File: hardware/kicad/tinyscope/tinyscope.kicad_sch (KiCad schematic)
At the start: 4 parts, among them J1 USB_C_Receptacle_USB2.0, U1 USBLC6-2SC6_MOD

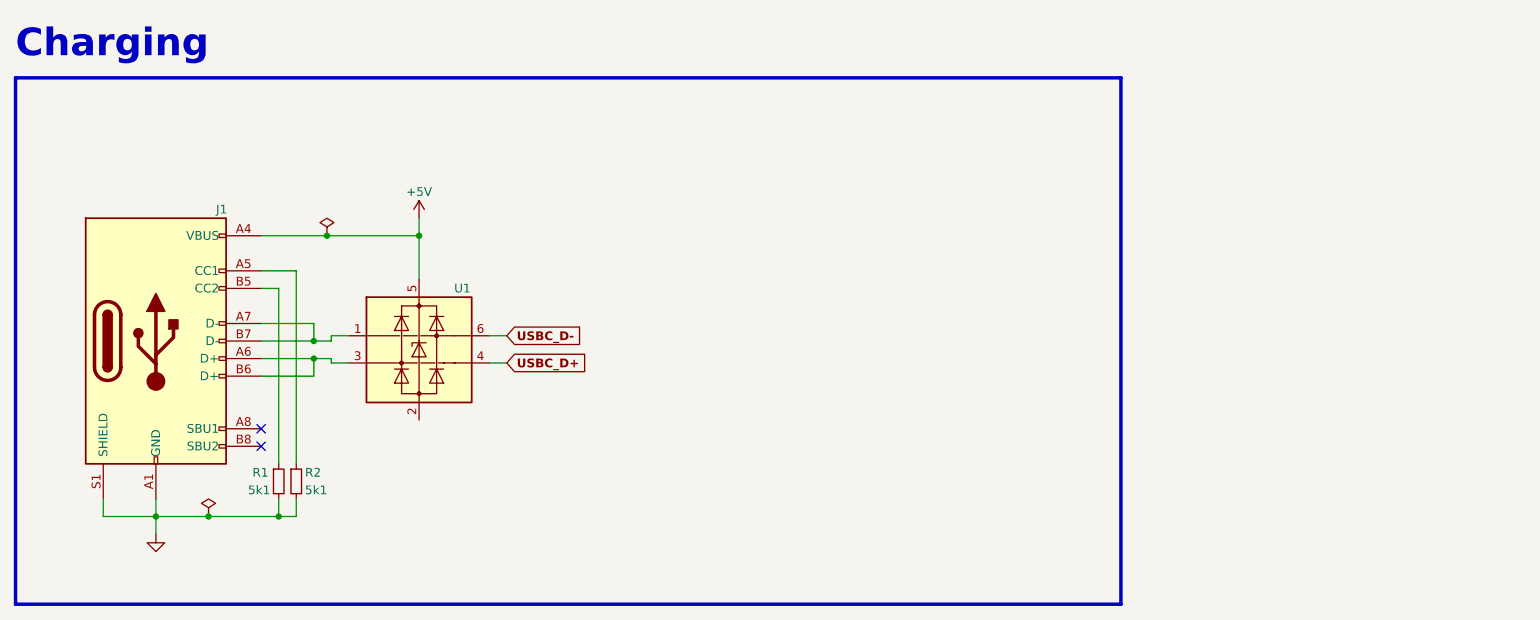
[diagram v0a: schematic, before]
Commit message: feat: hardware: Add tinyscope kicad project. Add USBC friendly battery charger part
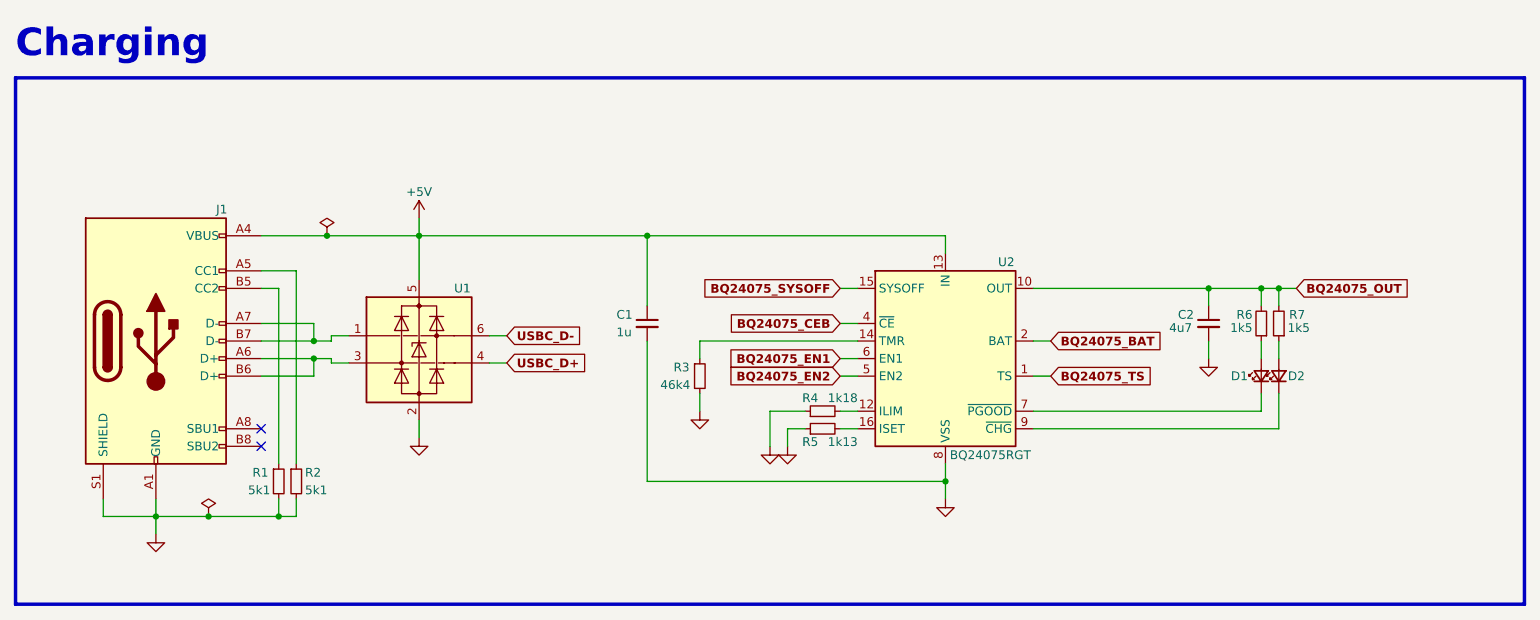
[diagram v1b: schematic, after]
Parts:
- added C1: 1u, symbol Device:C_Small
- added C2: 4u7, symbol Device:C_Small
- added D1, D2: LED_Small, symbol Device:LED_Small
- added R3: 46k4, symbol Device:R_Small
- added R4: 1k18, symbol Device:R_Small
- added R5: 1k13, symbol Device:R_Small
- added R6, R7: 1k5, symbol Device:R_Small
- added U2: BQ24075RGT, Package_DFN_QFN:VQFN-16-1EP_3x3mm_P0.5mm_EP1.6x1.6mm, symbol Battery_Management:BQ24075RGT
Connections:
- net +5V: now also C1.1, U2.13 (IN)
- net GND: now also U1.2 (GND), C1.2, C2.2, R3.2, R4.1, R5.1, U2.17 (VSS), U2.8 (VSS)
- new net: R5.2, U2.16 (ISET)
- new net: R4.2, U2.12 (ILIM)
- new net: R3.1, U2.14 (TMR)
- new net: D1.1 (K), U2.7 (~{PGOOD})
- new net: D2.1 (K), U2.9 (~{CHG})
- new net: D1.2 (A), R6.1
- new net: D2.2 (A), R7.1
- new net BQ24075_BAT: U2.2 (BAT), U2.3 (BAT)
- new net BQ24075_CEB: U2.4 (~{CE})
- new net BQ24075_EN1: U2.6 (EN1)
- new net BQ24075_EN2: U2.5 (EN2)
- new net BQ24075_OUT: C2.1, R6.2, R7.2, U2.10 (OUT), U2.11 (OUT)
- new net BQ24075_SYSOFF: U2.15 (SYSOFF)
- new net BQ24075_TS: U2.1 (TS)

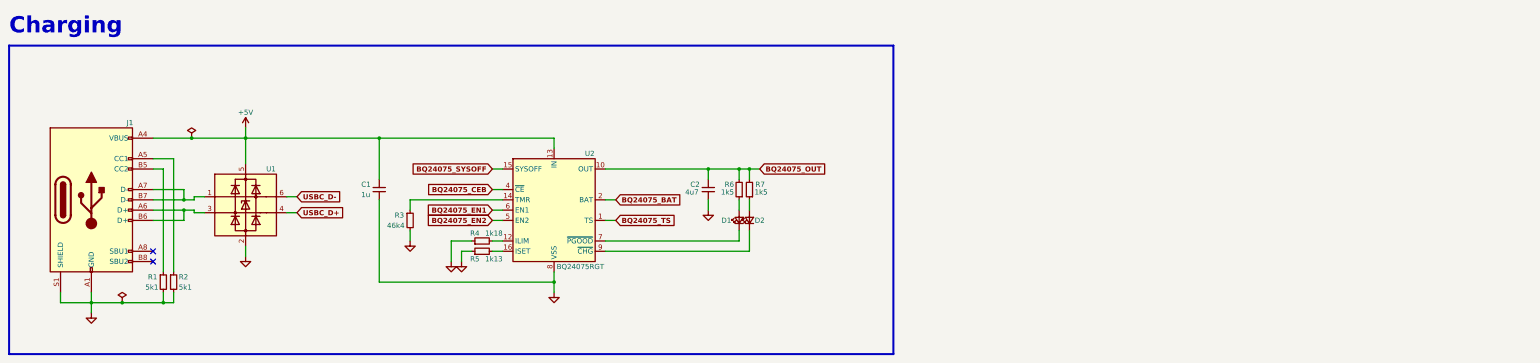
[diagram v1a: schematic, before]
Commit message: feat: hardware: Add tinyscope kicad project. Add fuel gauge part
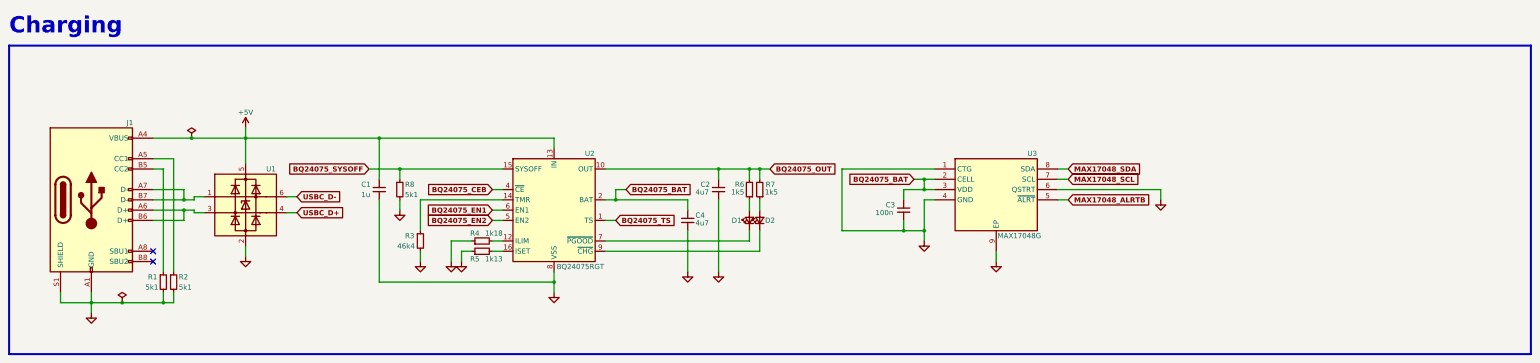
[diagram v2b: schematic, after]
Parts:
- added C3: 100n, symbol Device:C_Small
- added C4: 4u7, symbol Device:C_Small
- added R8: 5k1, symbol Device:R_Small
- added U3: MAX17048G, SON50P200X200X80-9N-D, symbol MAX17048G+T10:MAX17048G+T10
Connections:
- net BQ24075_BAT: now also C3.1, C4.1, U3.2 (CELL), U3.3 (VDD)
- net BQ24075_SYSOFF: now also R8.1
- net GND: now also C3.2, C4.2, R8.2, U3.1 (CTG), U3.4 (GND), U3.6 (QSTRT), U3.9 (EP)
- new net MAX17048_ALRTB: U3.5 (~{ALRT})
- new net MAX17048_SCL: U3.7 (SCL)
- new net MAX17048_SDA: U3.8 (SDA)
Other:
- moved on the sheet: C2, D1, D2, R3, R6, R7

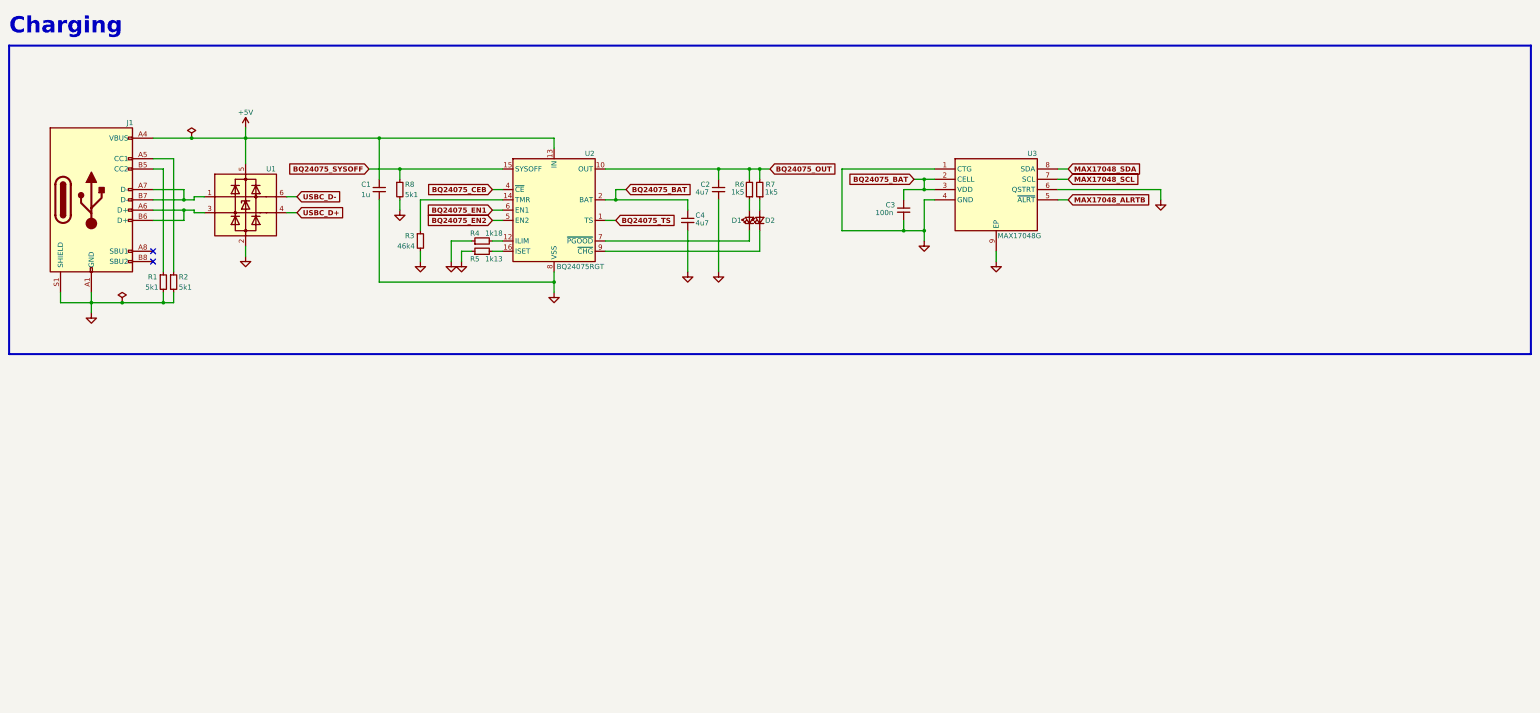
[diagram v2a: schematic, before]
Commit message: feat: hardware: Add tinyscope kicad project. Replace global labels with net labels
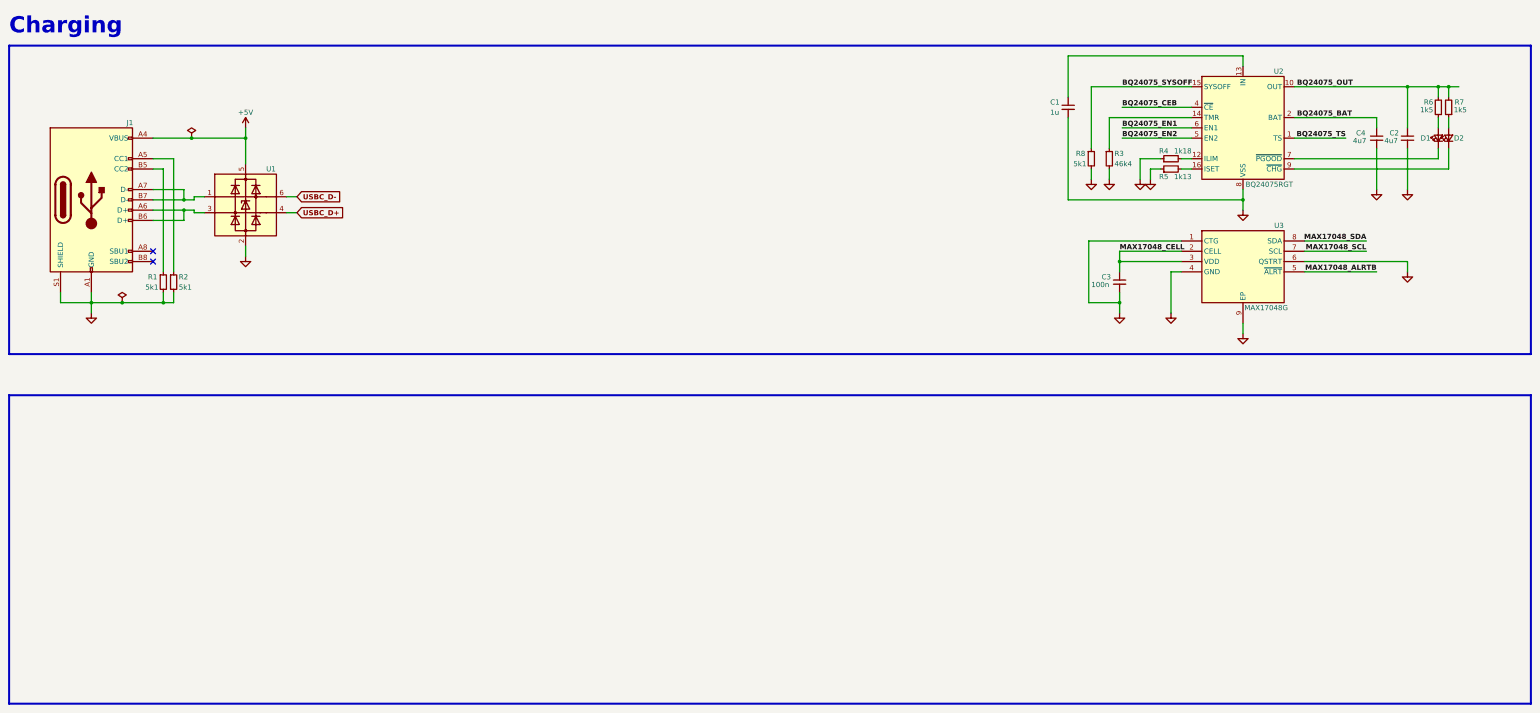
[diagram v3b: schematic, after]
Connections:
- net +5V: no longer C1.1, U2.13 (IN)
- net BQ24075_BAT: no longer C3.1, U3.2 (CELL), U3.3 (VDD)
- new net: C1.1, U2.13 (IN)
- new net MAX17048_CELL: C3.1, U3.2 (CELL), U3.3 (VDD)
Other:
- moved on the sheet: C1, C2, C3, C4, D1, D2, R3, R4, R5, R6, R7, R8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

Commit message: feat: hardware: Add tinyscope kicad project. Add TPS54360 buck converter for battery #1
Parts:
- added C10: 6800p, symbol Device:C_Small
- added C11: 39p, symbol Device:C_Small
- added C5, C6: 2u2, symbol Device:C_Small
- added C7: 100n, symbol Device:C_Small
- added C8, C9: 47u, symbol Device:C_Small
- added D3, D4: D_Schottky_Small, symbol Device:D_Schottky_Small
- added D5: D_Small, symbol Device:D_Small
- added L1: 8u2, symbol Device:L_Small
- added R10: 84k5, symbol Device:R_Small
- added R11: 162k, symbol Device:R_Small
- added R12: 13k, symbol Device:R_Small
- added R9: 523k, symbol Device:R_Small
- added U4: TPS54360DDA, Package_SO:TI_SO-PowerPAD-8_ThermalVias, symbol Regulator_Switching:TPS54360DDA
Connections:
- net +5V: now also D3.1 (K), D4.1 (K); no longer J1.A4 (VBUS), J1.A9 (VBUS), J1.B4 (VBUS), J1.B9 (VBUS), U1.5 (VBUS)
- net GND: now also C10.2, C11.2, C5.2, C6.2, C8.2, C9.2, D5.2 (A), R10.2, R11.2, U4.7 (GND), U4.9 (GNDPAD)
- new net: C11.1, R12.1, U4.6 (COMP)
- new net: C10.1, R12.2
- new net: C8.1, C9.1, L1.2
- new net: C7.2, D5.1 (K), L1.1, U4.8 (SW)
- new net: R10.1, R9.2, U4.3 (EN)
- new net: C7.1, U4.1 (BOOT)
- new net: R11.1, U4.4 (RT/CLK)
- new net +BATT: C5.1, C6.1, R9.1, U4.2 (VIN)
- new net TPS54360_FB: U4.5 (FB)
- new net VBUS: D4.2 (A), J1.A4 (VBUS), J1.A9 (VBUS), J1.B4 (VBUS), J1.B9 (VBUS), U1.5 (VBUS)

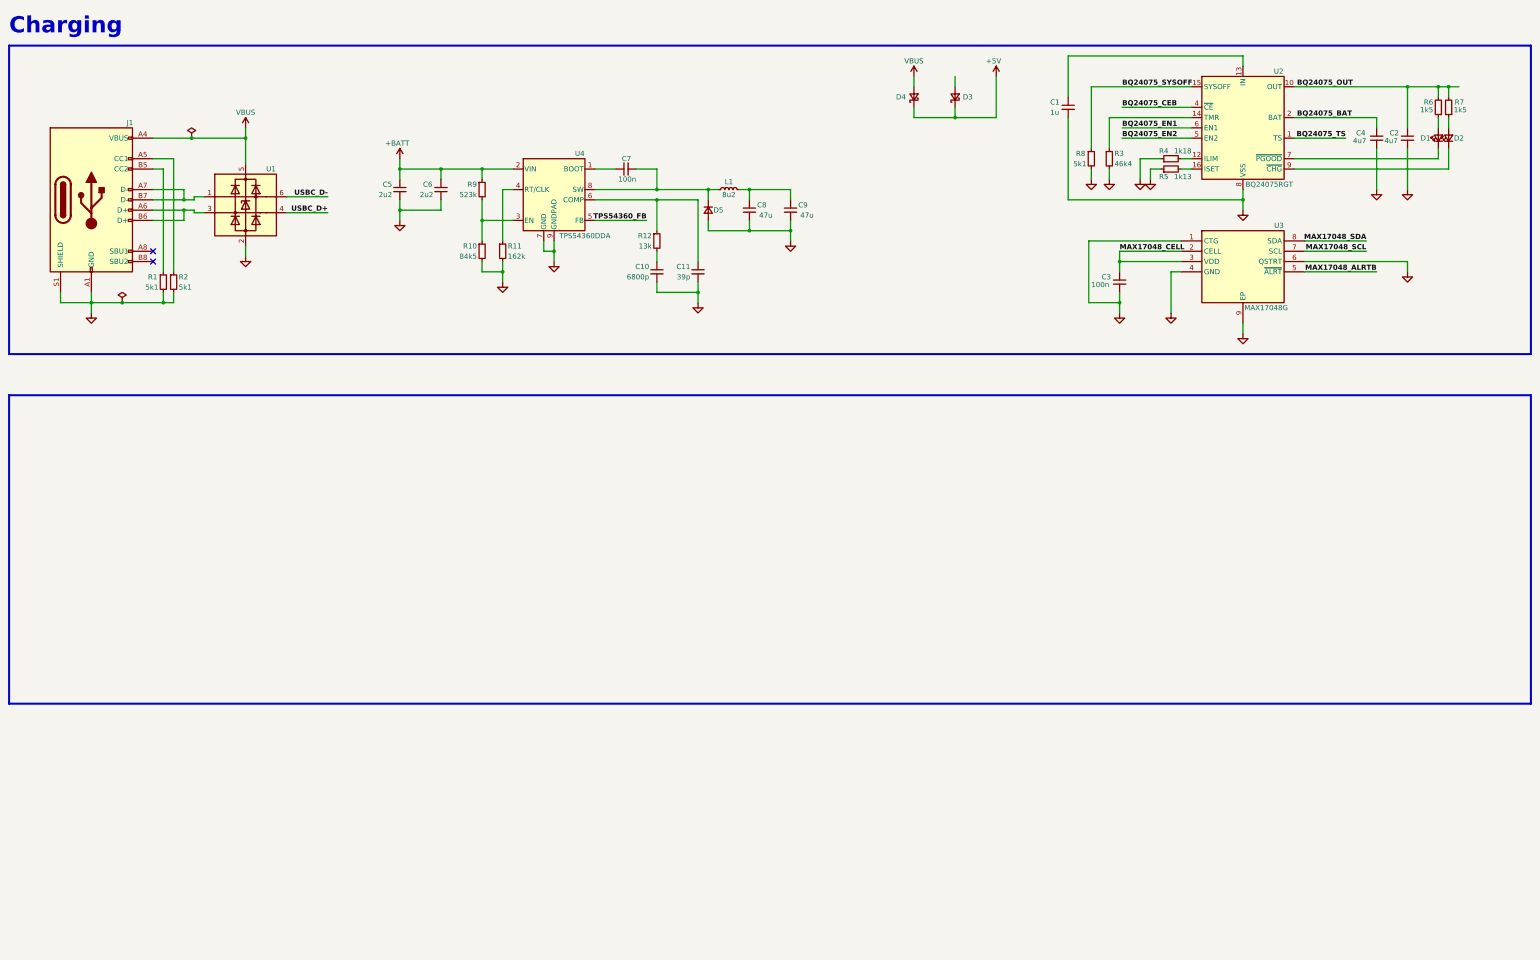
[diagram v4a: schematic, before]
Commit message: feat: hardware: Add tinyscope kicad project. Add TPS54360 buck converter for battery #2. Add reverse-polarity and transient protection
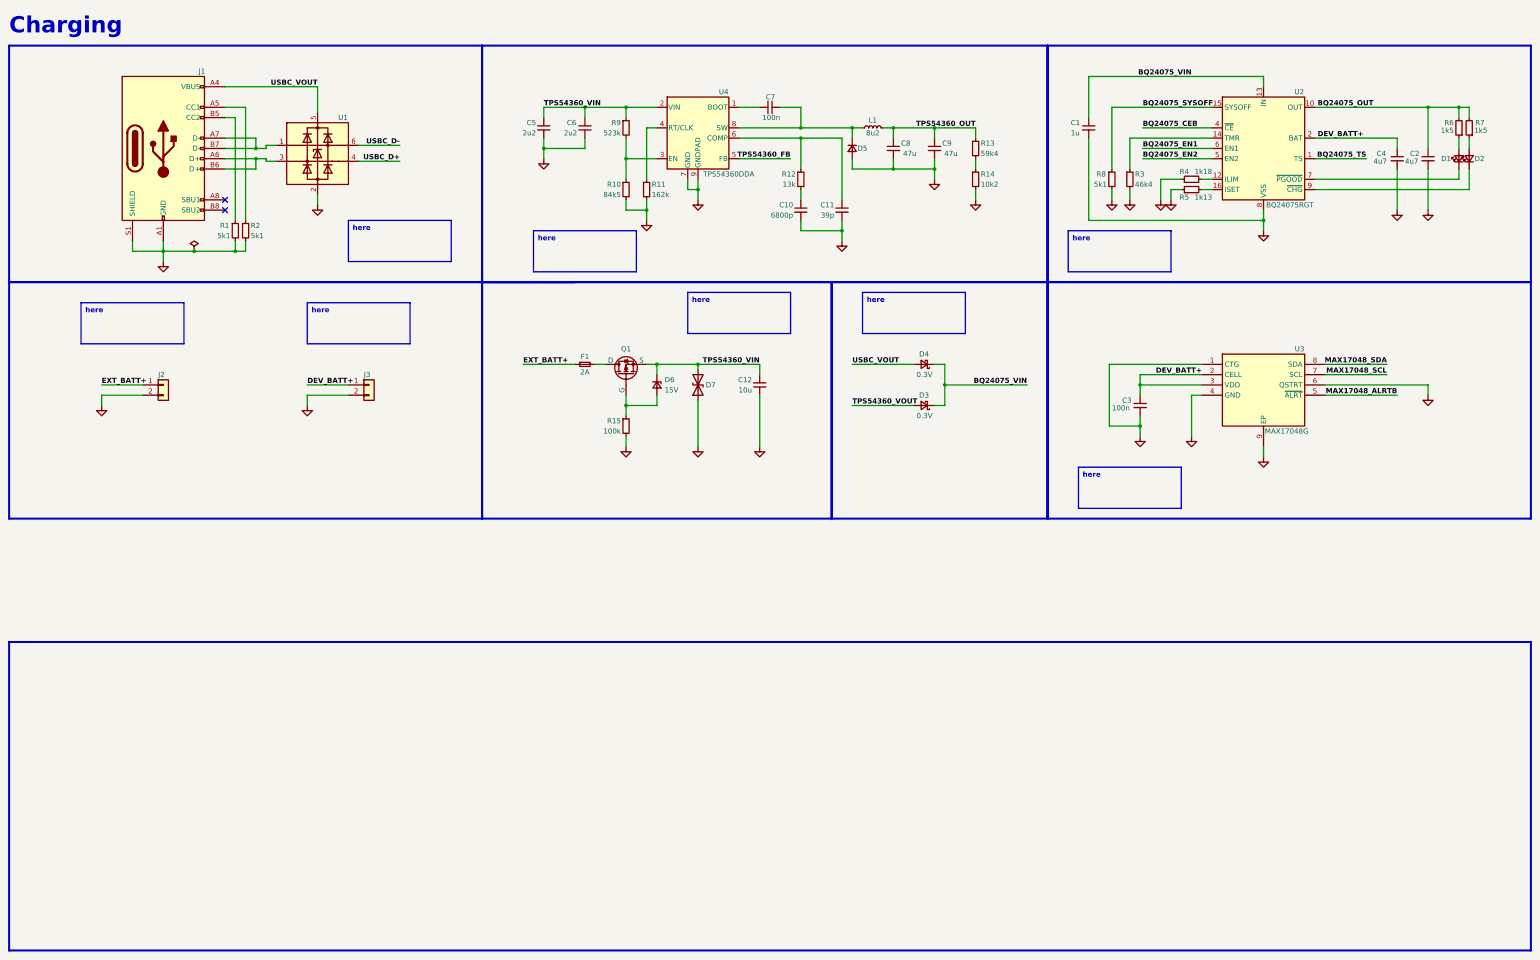
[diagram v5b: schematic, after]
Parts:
- added C12: 10u, symbol Device:C_Small
- added D6: 15V, symbol Device:D_Zener_Small
- added D7: D_TVS, symbol Device:D_TVS
- added F1: 2A, symbol Device:Fuse_Small
- added J2, J3: Conn_01x02, symbol Connector_Generic:Conn_01x02
- added Q1: PMOS, symbol Simulation_SPICE:PMOS
- added R13: 59k4, symbol Device:R_Small
- added R14: 10k2, symbol Device:R_Small
- added R15: 100k, symbol Device:R_Small
- D3, D4: value D_Schottky_Small -> 0.3V
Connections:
- net +5V is gone; now on net BQ24075_VIN: D3.1 (K), D4.1 (K)
- net MAX17048_CELL is gone; now on net DEV_BATT+: C3.1, U3.2 (CELL), U3.3 (VDD)
- net GND: now also C12.2, D7.1 (A1), J2.2 (Pin_2), J3.2 (Pin_2), R14.2, R15.2
- net TPS54360_OUT: now reaches C8.1, C9.1, L1.2
- net TPS54360_OUT: now also R13.1
- net TPS54360_VOUT: now reaches D3.2 (A)
- net BQ24075_VIN: now reaches C1.1, U2.13 (IN)
- net +BATT renamed TPS54360_VIN
- net TPS54360_VIN: now also C12.1, D6.1 (K), D7.2 (A2), Q1.3 (S)
- net BQ24075_BAT renamed DEV_BATT+
- net DEV_BATT+: now also J3.1 (Pin_1)
- net VBUS renamed USBC_VOUT
- new net: F1.2, Q1.1 (D)
- new net: R13.2, R14.1
- new net: D6.2 (A), Q1.2 (G), R15.1
- new net EXT_BATT+: F1.1, J2.1 (Pin_1)
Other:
- moved on the sheet: C1, C10, C11, C2, C3, C4, C5, C6, C7, C8, C9, D1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

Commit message: feat: hardware: Add tinyscope kicad project. Adds description blocks for Power Input & Charging section
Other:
- note added: "Power Input & Charging"
- note removed: "Charging"
- moved on the sheet: C1, C10, C11, C2, C4, C5, C6, C7, C8, C9, D1, D2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
